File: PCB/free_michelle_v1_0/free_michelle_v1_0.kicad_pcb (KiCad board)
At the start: 2 copper layers, 101 parts, among them J1 Zworka_TX, J10 ARK, J11 ARK, J12 Zworka_Buzzer, J13 ARK, J14 ARK, J15 Gniazdo 5VP DC 5,5x2,5, J16 Gniazdo 9V DC 5,5x2,5, J2 Zworka_RX, J3 GROVE_SW, J4 ARK, J5 ARK, J6 ARK, J7 ARK, J8 GROVE_SW, J9 A02YYUW_GroveCON, K1 FINDER-36.11, K2 FINDER-36.11, K3 FINDER-36.11, K4 FINDER-36.11, K5 FINDER-36.11, K6 FINDER-36.11, K7 FINDER-36.11, K8 FINDER-36.11, Q1 MMBT4403_PNP, Q2 MMBT4403_PNP, Q3 MMBT4403_PNP, Q4 MMBT4403_PNP, Q5 BSS138, Q6 MMBT4403_PNP, Q7 MMBT4403_PNP, Q8 MMBT4403_PNP, Q9 MMBT4403_PNP, SW1 Rotary_Encoder, SW2 SW_Push, SW3 SW_Push, U1 EEPROM_24AA01, U2 ESP8266_NodeMCU_v2, U3 DS3231M_RTC, U4 NRF24L01_Breakout, U5 BMP280, U6 LD1117V33, U7 L7805, U8 LD1117V33

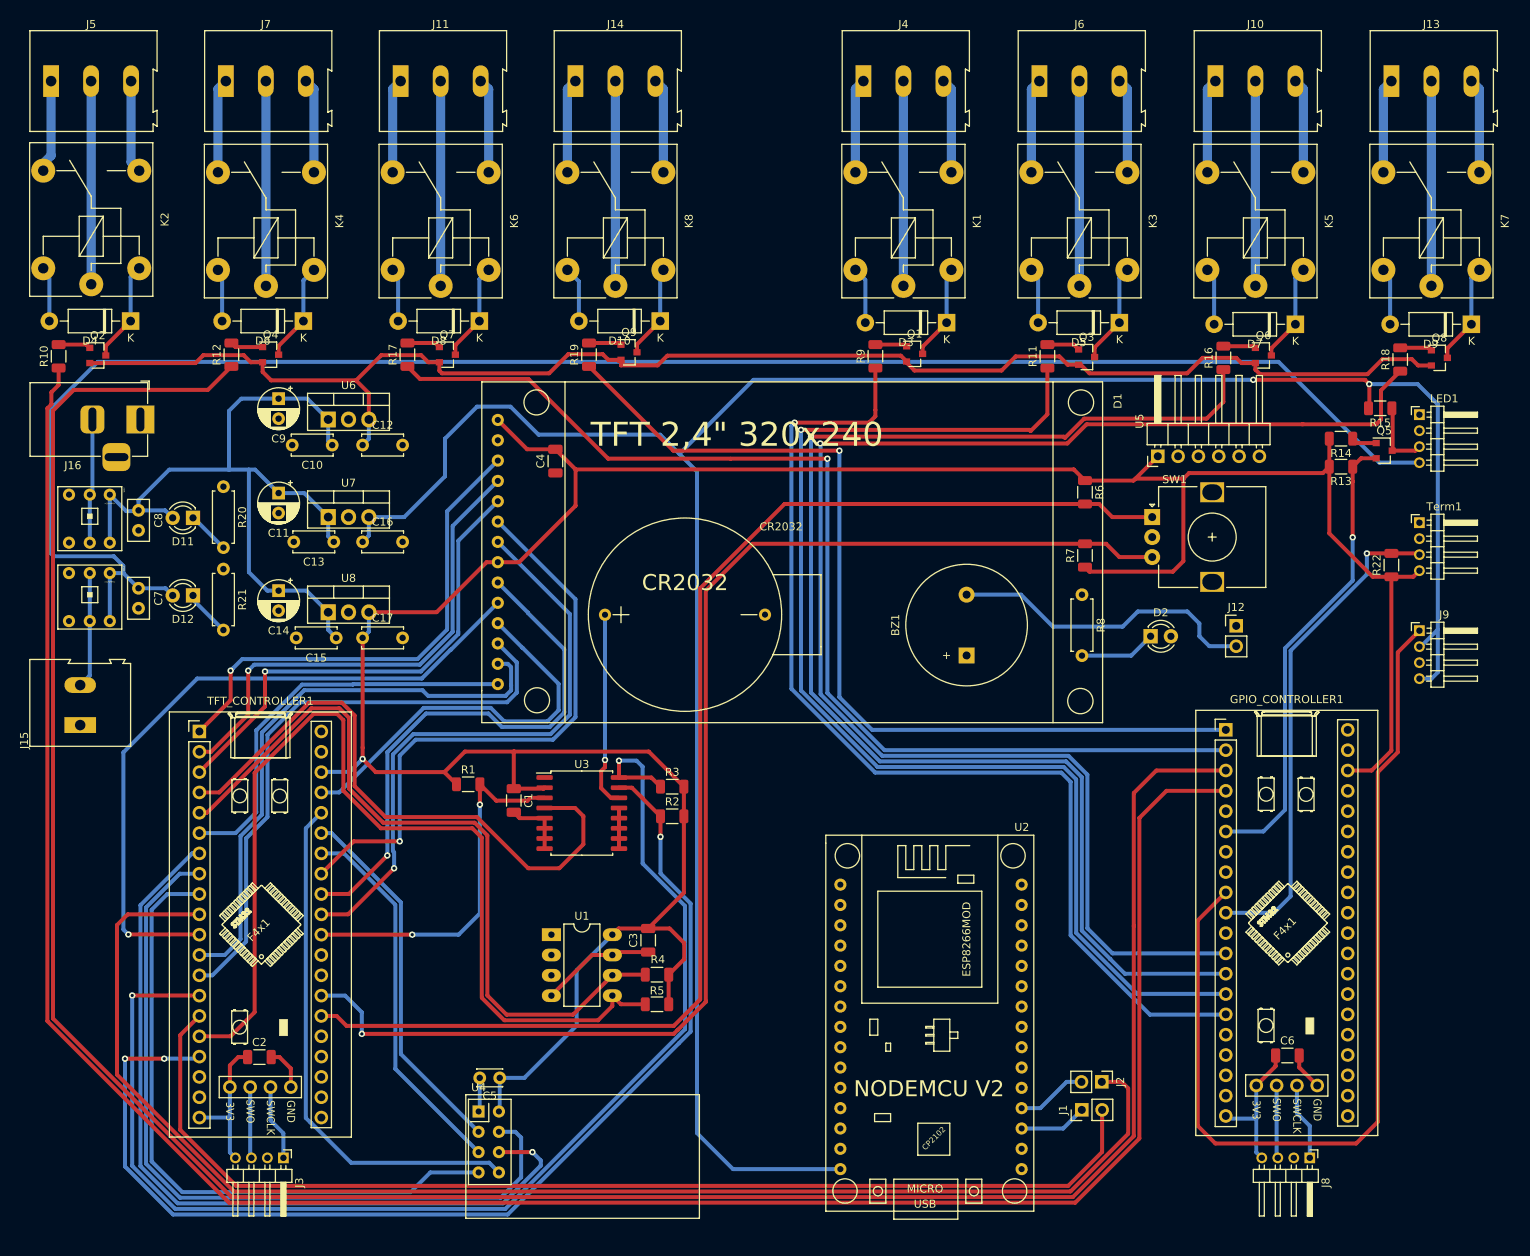
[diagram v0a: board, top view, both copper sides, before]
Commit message: Wylano pola masy na obu stronach PCB
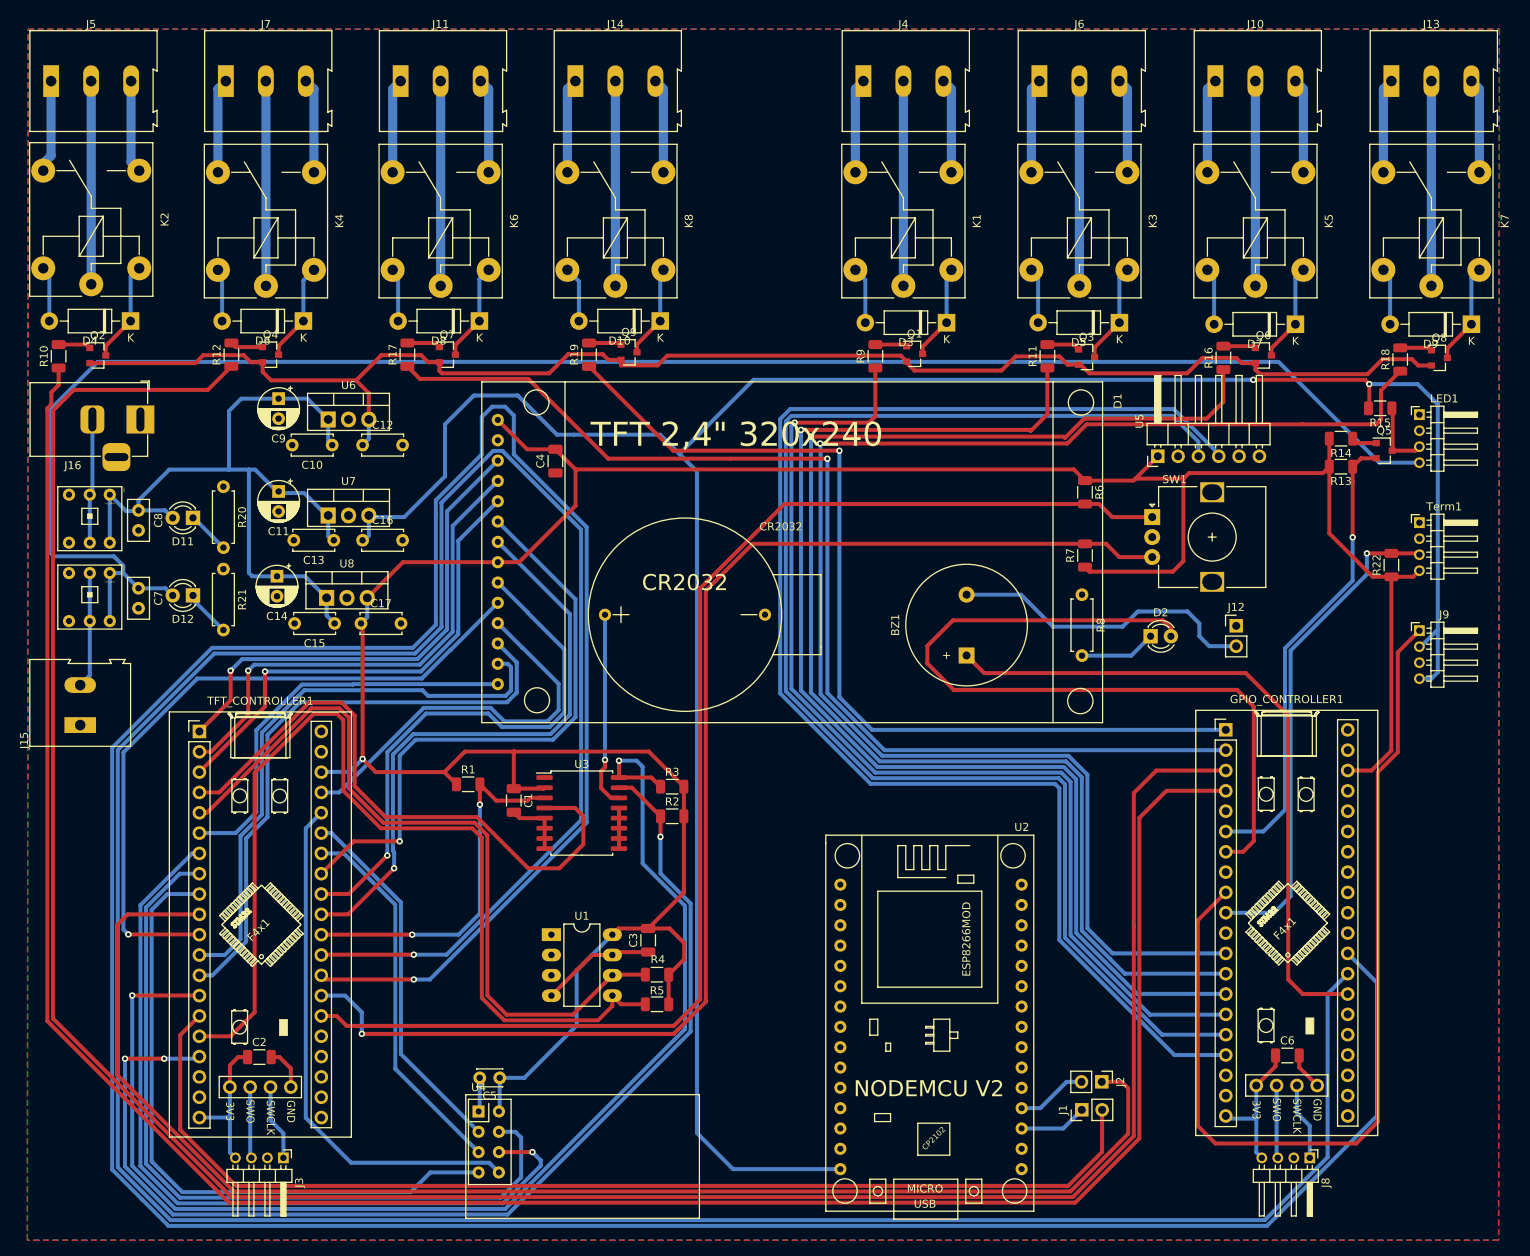
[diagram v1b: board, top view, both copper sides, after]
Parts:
- moved C14 1.81 mm to (56.2, 84.1)
- moved C15 1.81 mm to (63.4, 90.0)
- moved C17 1.81 mm to (66.7, 90.0)
- moved U8 1.81 mm to (62.4, 86.8)
- moved C11 0.20 mm to (56.4, 73.5)
- moved C13 0.20 mm to (63.3, 79.6)
- moved C16 0.20 mm to (66.9, 79.6)
- moved U7 0.20 mm to (62.6, 76.5)
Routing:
- net Net-(GPIO_CONTROLLER1-Pad9): track 0.00 -> 417.6 mm, vias 0 -> 1
- net Net-(GPIO_CONTROLLER1-Pad8): track 0.00 -> 395.7 mm, vias 0 -> 1
- net BMP_SDA_PB9: track 0.00 -> 177.8 mm
- net BMP_SCL_PB8: track 0.00 -> 172.8 mm
- net USER_LED_PA10: track 0.00 -> 99.2 mm
- net Buzzer_PA1: track 0.00 -> 84.5 mm
- net +5V: track 301.6 -> 303.8 mm
- net +3V3: track 408.5 -> 409.8 mm
- net +9V: track 100.8 -> 99.9 mm
- added copper zone on B.Cu, net GND
- added copper zone on F.Cu, net GND

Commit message: Dodane napisy i otwory montarzowe pod TFT
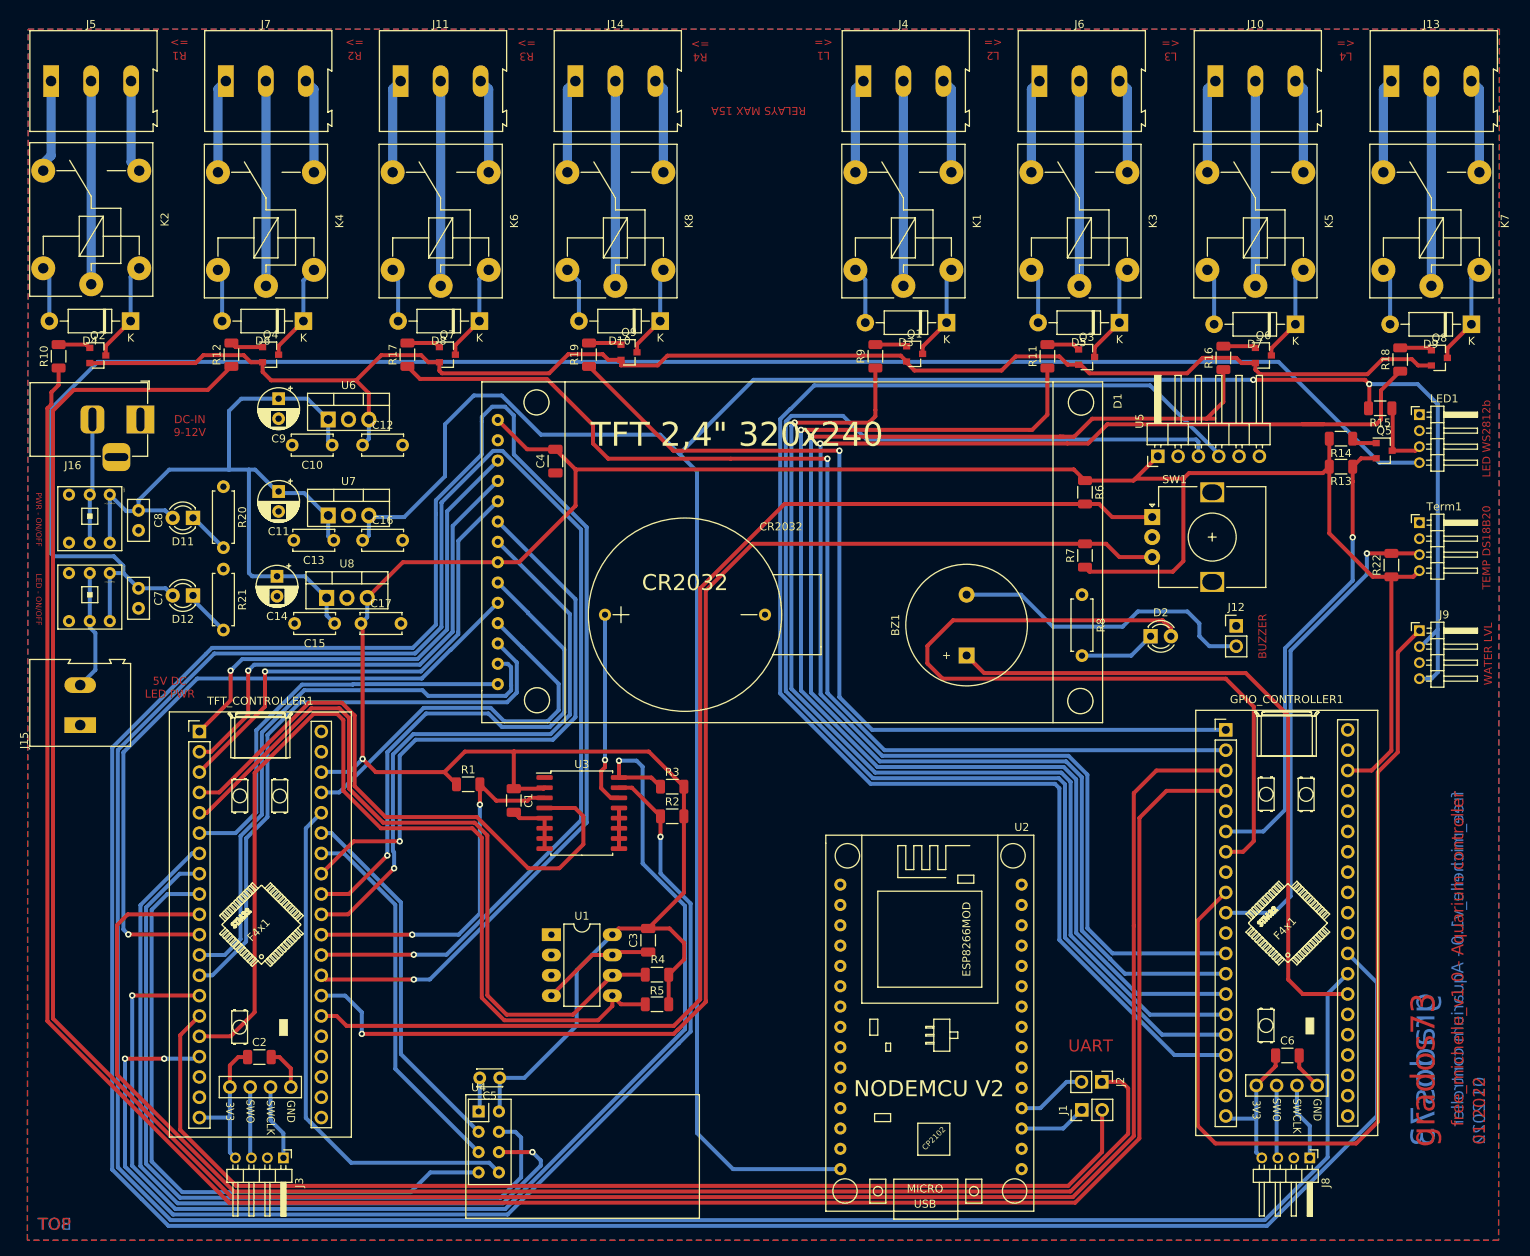
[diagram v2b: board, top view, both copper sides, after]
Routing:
- net LIGHT4_PB4: track 185.3 -> 187.9 mm
- net BMP_SDA_PB9: track 177.8 -> 180.2 mm
- net LIGHT3_PB5: track 167.2 -> 168.5 mm
- net RELAY3_PB13: track 139.3 -> 140.7 mm
- net Net-(J15-Pad2): track 14.5 -> 15.1 mm
- net GND: vias 0 -> 4
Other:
- board text added: "01.2022"
- board text added: "5V DC LED PWR"
- board text added: "BOT"
- board text added: "BUZZER"
- board text added: "DC-IN 9-12V"
- board text added: "L1 <="
- board text added: "L2 <="
- board text added: "L3 <="
- board text added: "L4 <="
- board text added: "LED - ON/OFF"
- board text added: "LED WS2812b"
- board text added: "PWR - ON/OFF"
- board text added: "R1 =>"
- board text added: "R2 =>"
- board text added: "R3 =>"
- board text added: "R4 =>"
- board text added: "RELAYS MAX 15A"
- board text added: "TEMP DS18B20"
- board text added: "TOP"
- board text added: "UART"
- board text added: "WATER LVL"
- board text added: "free_michelle_v1.0 - Aquarium controller"
- board text added: "grados73"

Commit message: Gotowa płytka przed generacją gerberow
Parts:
- added H1: MountingHole, MountingHole:MountingHole_3.2mm_M3, F.Cu at (201.1, 163.0)
- added H2: MountingHole, MountingHole:MountingHole_3.2mm_M3, F.Cu at (34.5, 163.0)
- added H3: MountingHole, MountingHole:MountingHole_3.2mm_M3, F.Cu at (43.7, 52.8)
- added H4: MountingHole, MountingHole:MountingHole_3.2mm_M3, F.Cu at (189.4, 52.8)
- U6, U8: value LD1117V33 -> LD1117AV33
- moved U8 5.68 mm to (67.6, 84.6), turned to 180 degrees
- moved U6 5.28 mm to (67.5, 62.5), turned to 180 degrees
- moved C9 1.40 mm to (55.0, 62.0)
- moved C11 1.40 mm to (55.0, 73.4)
- moved C14 1.21 mm to (55.0, 84.3)
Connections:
- U6 pad 1: +9V -> GND
- U6 pad 2: GND -> +3.3VP
- U6 pad 3: +3.3VP -> +9V
- U8 pad 1: +9V -> GND
- U8 pad 2: GND -> +3V3
- U8 pad 3: +3V3 -> +9V
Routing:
- net +9V: track 99.9 -> 105.0 mm
- net +3V3: track 409.8 -> 414.7 mm
- net LIGHT3_PB5: track 168.5 -> 167.9 mm
- net GND: vias 4 -> 79
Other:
- board outline added: 183.9 x 151.3 mm
